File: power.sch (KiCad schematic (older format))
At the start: 7 parts, among them U2 LM2776, U3 LT1761-5

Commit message: Get rid of hand-soldering footprints in schematic too
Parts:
- C1, C2, C4, C5, C6: footprint Capacitor_SMD:C_0603_1608Metric_Pad1.05x0.95mm_HandSolder -> Capacitor_SMD:C_0603_1608Metric
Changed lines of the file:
@@
 $Descr A4 11693 8268
 encoding utf-8
-Sheet 5 5
+Sheet 4 5
 Title ""
 Date ""
@@
 F 0 "C6" H 6986 3596 50  0000 R CNN
 F 1 "1u" H 6986 3505 50  0000 R CNN
-F 2 "Capacitor_SMD:C_0603_1608Metric_Pad1.05x0.95mm_HandSolder" H 7138 3400 50  0001 C CNN
+F 2 "Capacitor_SMD:C_0603_1608Metric" H 7138 3400 50  0001 C CNN
 F 3 "~" H 7100 3550 50  0001 C CNN
 	1    7100 3550
@@
 F 0 "C5" H 5935 3404 50  0000 R CNN
 F 1 "0.01u" H 5935 3495 50  0000 R CNN
-F 2 "Capacitor_SMD:C_0603_1608Metric_Pad1.05x0.95mm_HandSolder" H 6088 3300 50  0001 C CNN
+F 2 "Capacitor_SMD:C_0603_1608Metric" H 6088 3300 50  0001 C CNN
 F 3 "~" H 6050 3450 50  0001 C CNN
 	1    6050 3450
@@
 F 0 "C2" H 5186 3746 50  0000 R CNN
 F 1 "1u" H 5186 3655 50  0000 R CNN
-F 2 "Capacitor_SMD:C_0603_1608Metric_Pad1.05x0.95mm_HandSolder" H 5338 3550 50  0001 C CNN
+F 2 "Capacitor_SMD:C_0603_1608Metric" H 5338 3550 50  0001 C CNN
 F 3 "~" H 5300 3700 50  0001 C CNN
 	1    5300 3700
@@
 F 0 "C1" H 3835 3654 50  0000 R CNN
 F 1 "2.2u" H 3835 3745 50  0000 R CNN
-F 2 "Capacitor_SMD:C_0603_1608Metric_Pad1.05x0.95mm_HandSolder" H 3988 3550 50  0001 C CNN
+F 2 "Capacitor_SMD:C_0603_1608Metric" H 3988 3550 50  0001 C CNN
 F 3 "~" H 3950 3700 50  0001 C CNN
 	1    3950 3700
@@
 F 0 "C4" H 5435 3654 50  0000 R CNN
 F 1 "2.2u" H 5435 3745 50  0000 R CNN
-F 2 "Capacitor_SMD:C_0603_1608Metric_Pad1.05x0.95mm_HandSolder" H 5588 3550 50  0001 C CNN
+F 2 "Capacitor_SMD:C_0603_1608Metric" H 5588 3550 50  0001 C CNN
 F 3 "~" H 5550 3700 50  0001 C CNN
 	1    5550 3700

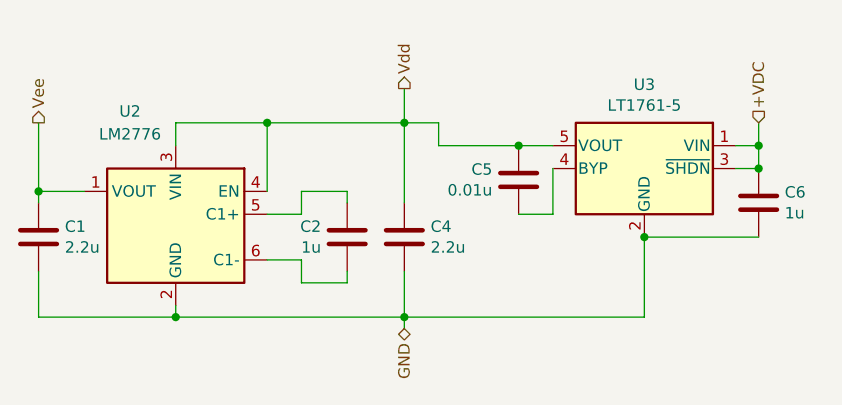
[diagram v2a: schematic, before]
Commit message: Use a big 47uF cap on input to regulator
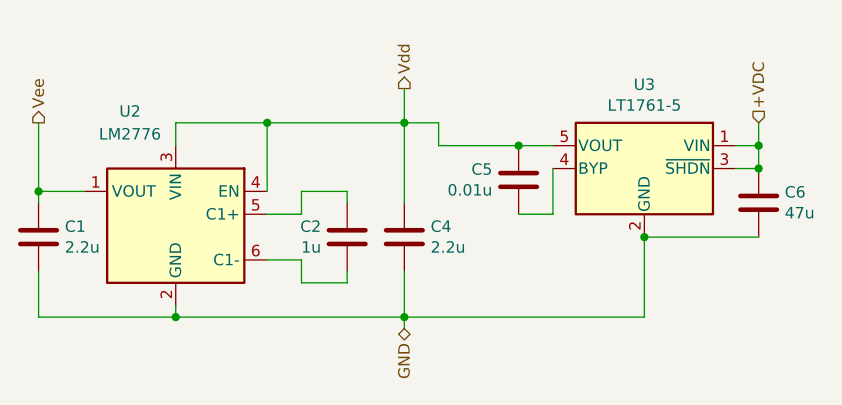
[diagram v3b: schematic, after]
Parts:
- C6: value 1u -> 47u; footprint Capacitor_SMD:C_0603_1608Metric -> Capacitor_SMD:C_1206_3216Metric
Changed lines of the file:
@@
 AR Path="/5ECDCFC2/5ECE4C57" Ref="C6"  Part="1"
 F 0 "C6" H 6986 3596 50  0000 R CNN
-F 1 "1u" H 6986 3505 50  0000 R CNN
-F 2 "Capacitor_SMD:C_0603_1608Metric" H 7138 3400 50  0001 C CNN
-F 3 "~" H 7100 3550 50  0001 C CNN
+F 1 "47u" H 6986 3505 50  0000 R CNN
+F 2 "Capacitor_SMD:C_1206_3216Metric" H 7138 3400 50  0001 C CNN
+F 3 "https://octopart.com/c3216x5r1e476m160ac-tdk-25947783?r=sp" H 7100 3550 50  0001 C CNN
 	1    7100 3550
 	-1   0    0    -1

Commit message: Obey some ERC findings
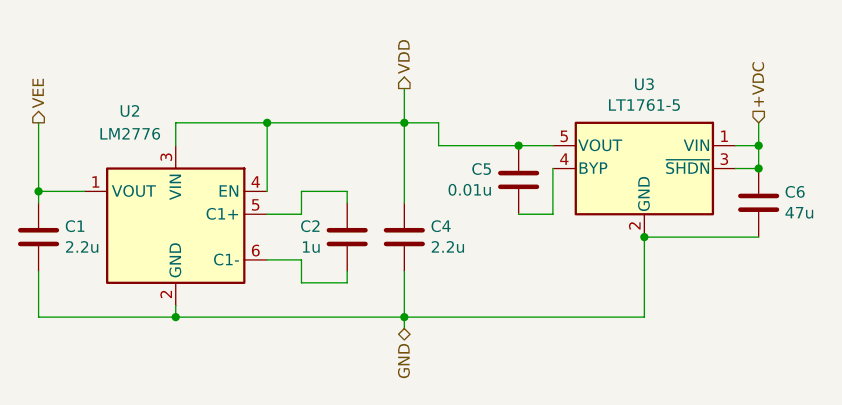
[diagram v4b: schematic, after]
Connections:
- net Vdd renamed VDD
- net Vee renamed VEE
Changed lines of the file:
@@
 $EndComp
 Text HLabel 3950 3200 1    50   Output ~ 0
-Vee
+VEE
 Text HLabel 5550 3050 1    50   Output ~ 0
-Vdd
+VDD
 Wire Wire Line
 	5550 3200 5550 3050

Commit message: Rearrange pins cosmetically
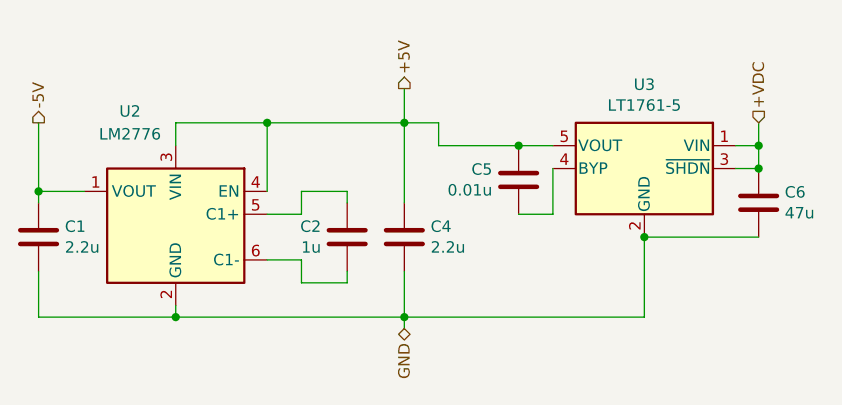
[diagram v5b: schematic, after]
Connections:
- net VDD renamed +5V
- net VEE renamed -5V
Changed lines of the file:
@@
 $EndComp
 Text HLabel 3950 3200 1    50   Output ~ 0
-VEE
+-5V
 Text HLabel 5550 3050 1    50   Output ~ 0
-VDD
++5V
 Wire Wire Line
 	5550 3200 5550 3050

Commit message: Adjust cosmetics of power schematic
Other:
- moved on the sheet: C5, C6
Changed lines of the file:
@@
 Wire Wire Line
 	5700 3200 5700 3300
-Wire Wire Line
-	6200 3600 6050 3600
-Wire Wire Line
-	6200 3400 6200 3600
-Wire Wire Line
-	7100 3700 6600 3700
 $Comp
 L Device:C C?
 U 1 1 5ECE4C57
-P 7100 3550
+P 7100 3700
 AR Path="/5ECE4C57" Ref="C?"  Part="1"
 AR Path="/5ECDCFC2/5ECE4C57" Ref="C6"  Part="1"
-F 0 "C6" H 6986 3596 50  0000 R CNN
-F 1 "47u" H 6986 3505 50  0000 R CNN
-F 2 "Capacitor_SMD:C_1206_3216Metric" H 7138 3400 50  0001 C CNN
-F 3 "https://octopart.com/c3216x5r1e476m160ac-tdk-25947783?r=sp" H 7100 3550 50  0001 C CNN
-	1    7100 3550
+F 0 "C6" H 6986 3746 50  0000 R CNN
+F 1 "47u" H 6986 3655 50  0000 R CNN
+F 2 "Capacitor_SMD:C_1206_3216Metric" H 7138 3550 50  0001 C CNN
+F 3 "https://octopart.com/c3216x5r1e476m160ac-tdk-25947783?r=sp" H 7100 3700 50  0001 C CNN
+	1    7100 3700
 	-1   0    0    -1
 $EndComp
 Wire Wire Line
-	6050 3300 5700 3300
-Wire Wire Line
-	6200 3300 6050 3300
-Connection ~ 6050 3300
-$Comp
-L Device:C C?
-U 1 1 5ECE4C60
-P 6050 3450
-AR Path="/5ECE4C60" Ref="C?"  Part="1"
-AR Path="/5ECDCFC2/5ECE4C60" Ref="C5"  Part="1"
-F 0 "C5" H 5935 3404 50  0000 R CNN
-F 1 "0.01u" H 5935 3495 50  0000 R CNN
-F 2 "Capacitor_SMD:C_0603_1608Metric" H 6088 3300 50  0001 C CNN
-F 3 "~" H 6050 3450 50  0001 C CNN
-	1    6050 3450
-	1    0    0    1
-$EndComp
-Wire Wire Line
-	7100 3200 7100 3300
+	7100 3050 7100 3300
 Wire Wire Line
 	7100 3300 7000 3300
@@
 Connection ~ 3950 3500
 Wire Wire Line
-	3950 3200 3950 3500
+	3950 3050 3950 3500
 $Comp
 L Device:C C?
@@
 Wire Wire Line
 	5550 4050 5550 4100
+Text HLabel 3950 3050 1    50   Output ~ 0
+-5V
+Text HLabel 5550 3050 1    50   Output ~ 0
++5V
+Wire Wire Line
+	5550 3200 5550 3050
+Wire Wire Line
+	6600 3700 6600 4050
+Wire Wire Line
+	6600 4050 5550 4050
+Text HLabel 5550 4100 3    50   BiDi ~ 0
+GND
+Text HLabel 7100 3050 1    50   Input ~ 0
++VDC
+Wire Wire Line
+	6600 4050 7100 4050
+Wire Wire Line
+	7100 4050 7100 3850
+Connection ~ 6600 4050
+Wire Wire Line
+	7100 3550 7100 3400
+Wire Wire Line
+	5700 3300 6200 3300
+$Comp
+L Device:C C?
+U 1 1 5ECE4C60
+P 5950 3400
+AR Path="/5ECE4C60" Ref="C?"  Part="1"
+AR Path="/5ECDCFC2/5ECE4C60" Ref="C5"  Part="1"
+F 0 "C5" V 5790 3400 50  0000 C CNN
+F 1 "0.01u" V 5699 3400 50  0000 C CNN
+F 2 "Capacitor_SMD:C_0603_1608Metric" H 5988 3250 50  0001 C CNN
+F 3 "~" H 5950 3400 50  0001 C CNN
+	1    5950 3400
+	0    1    -1   0
+$EndComp
 $Comp
 L Device:C C?
@@
 	-1   0    0    1
 $EndComp
-Text HLabel 3950 3200 1    50   Output ~ 0
--5V
-Text HLabel 5550 3050 1    50   Output ~ 0
-+5V
 Wire Wire Line
-	5550 3200 5550 3050
+	6200 3400 6100 3400
 Wire Wire Line
-	6600 3700 6600 4050
+	5800 3400 5700 3400
 Wire Wire Line
-	6600 4050 5550 4050
-Connection ~ 6600 3700
-Text HLabel 5550 4100 3    50   BiDi ~ 0
-GND
-Text HLabel 7100 3200 1    50   Input ~ 0
-+VDC
+	5700 3400 5700 3300
+Connection ~ 5700 3300
 $EndSCHEMATC
